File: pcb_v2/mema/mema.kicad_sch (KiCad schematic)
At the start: 21 parts, among them J1 bus_mem_1, J2 bus_mem_2, J3 cartridge, U1 CY62256-70PC, U2 CY62256-70PC, U3 74LS283, U4 74LS00, U5 74LS32, U7 74LS138

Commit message: roteamento com problemas; refazer
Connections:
- net ~{rom_select} is gone; now on net rom_select: J3.3 (Pin_3)
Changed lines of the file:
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@@
 		)
 	)
-	(global_label "~{rom_select}"
+	(global_label "rom_select"
 		(shape input)
 		(at 30.48 87.63 180)

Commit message: concluído o roteamento
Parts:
- J1: value bus_mem_1 -> bus mem 1
- J2: value bus_mem_2 -> bus mem 2
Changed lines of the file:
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@@
 			)
 		)
-		(property "Value" "bus_mem_1"
+		(property "Value" "bus mem 1"
 			(at 35.56 29.21 0)
 			(effects
@@
 			)
 		)
-		(property "Value" "bus_mem_2"
+		(property "Value" "bus mem 2"
 			(at 77.47 29.21 0)
 			(effects

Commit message: experimentação com opcodes
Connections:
- net data_{0}: now also J1.14 (Pin_14); no longer J1.4 (Pin_4)
- net data_{1}: now also J1.13 (Pin_13); no longer J1.3 (Pin_3)
- net data_{2}: now also J1.11 (Pin_11); no longer J1.5 (Pin_5)
- net data_{3}: now also J1.9 (Pin_9); no longer J1.7 (Pin_7)
- net data_{4}: now also J1.7 (Pin_7); no longer J1.9 (Pin_9)
- net data_{5}: now also J1.5 (Pin_5); no longer J1.11 (Pin_11)
- net data_{6}: now also J1.3 (Pin_3); no longer J1.13 (Pin_13)
- net data_{7}: now also J1.4 (Pin_4); no longer J1.14 (Pin_14)

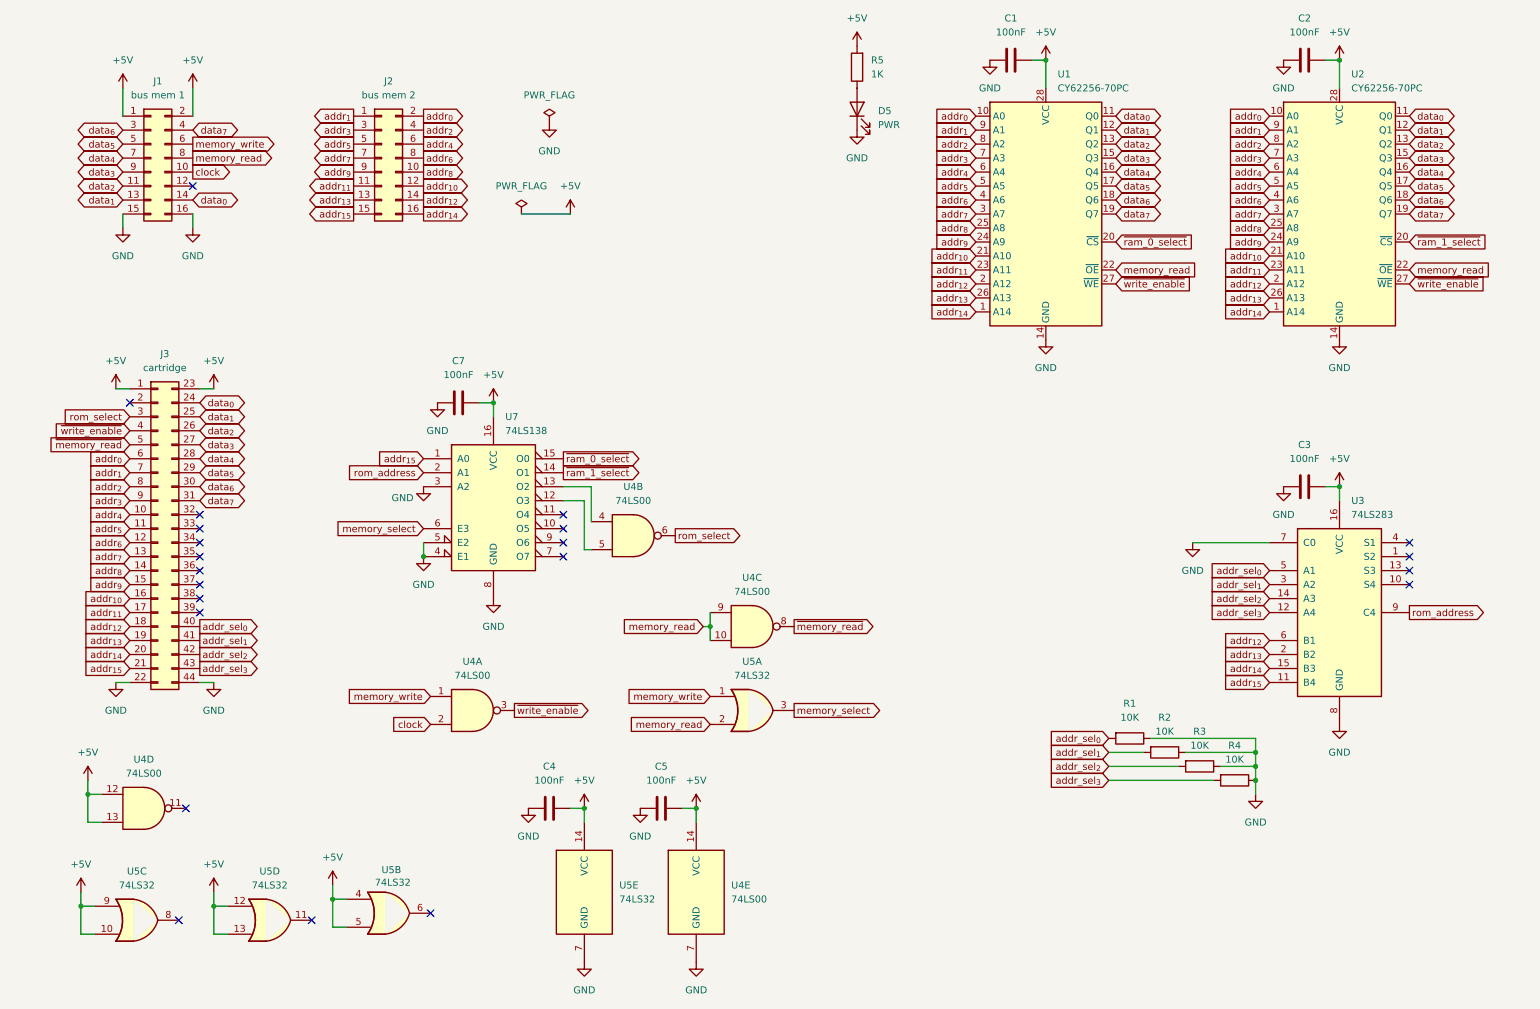
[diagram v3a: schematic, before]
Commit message: concluído o layout do pcb
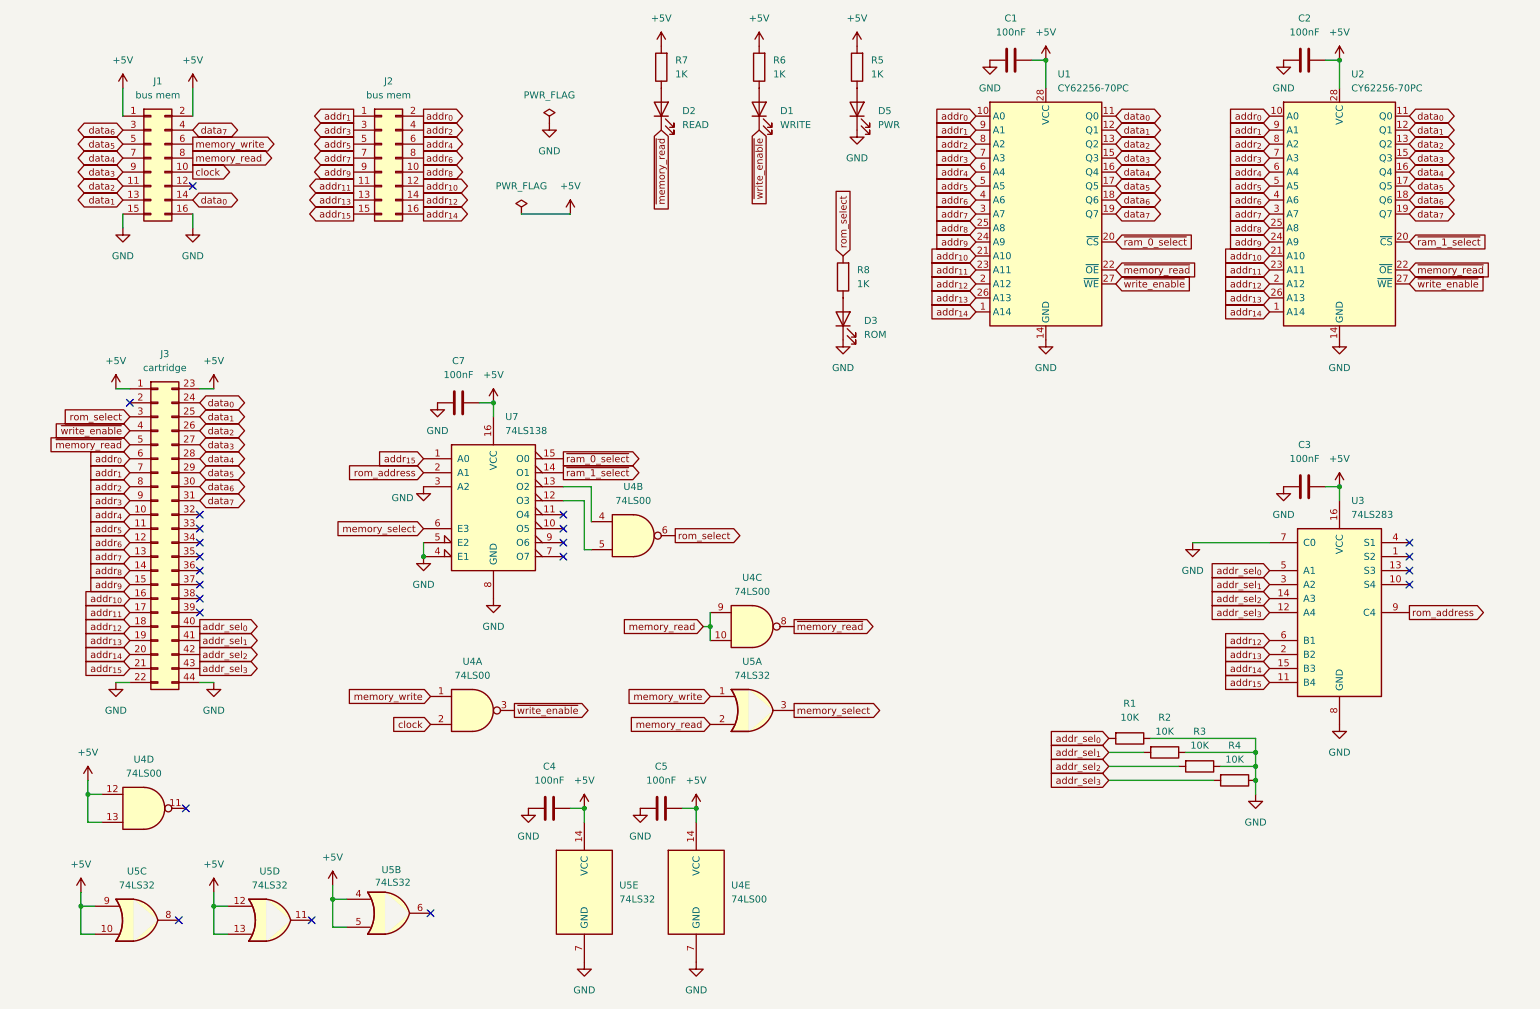
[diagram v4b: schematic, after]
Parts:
- added D1: WRITE, LED_THT:LED_D5.0mm, symbol Device:LED
- added D2: READ, LED_THT:LED_D5.0mm, symbol Device:LED
- added D3: ROM, LED_THT:LED_D5.0mm, symbol Device:LED
- added R6, R7, R8: 1K, Resistor_THT:R_Axial_DIN0207_L6.3mm_D2.5mm_P7.62mm_Horizontal, symbol Device:R
- J1: value bus mem 1 -> bus mem
- J2: value bus mem 2 -> bus mem
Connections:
- net +5V: now also R6.2, R7.2
- net GND: now also D3.1 (K)
- net memory_read: no longer U1.22 (~{OE}), U2.22 (~{OE})
- net rom_select: now also R8.2
- net ~{memory_read}: now also U1.22 (~{OE}), U2.22 (~{OE}), D2.1 (K)
- net ~{write_enable}: now also D1.1 (K)
- new net: D1.2 (A), R6.1
- new net: D3.2 (A), R8.1
- new net: D2.2 (A), R7.1
